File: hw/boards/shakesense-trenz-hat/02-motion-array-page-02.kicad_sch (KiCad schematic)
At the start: 4 parts, among them U14 LSM6DSOTR

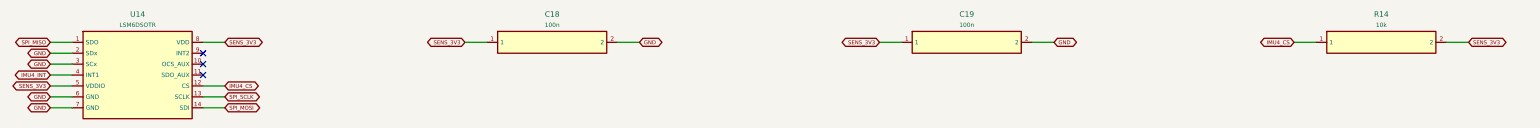
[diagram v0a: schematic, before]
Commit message: Expose Trenz GPIOs on the Pi-outline HDI sensor HAT
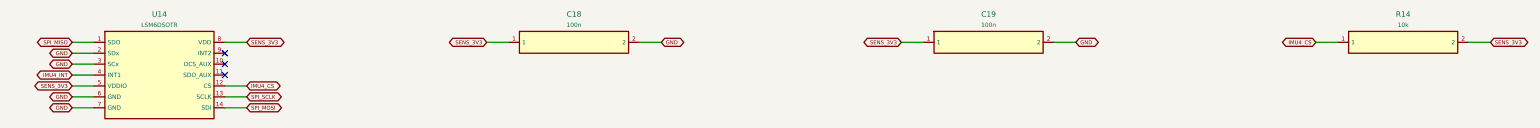
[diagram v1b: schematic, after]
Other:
- title: shakesense-trenz-hat / 02-motion-array-page-02 -> ShakeSense T1 / 02-motion-array-page-02
- moved on the sheet: C18, C19, R14, U14
